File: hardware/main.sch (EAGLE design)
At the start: 79 parts, among them U1 TMS320F28069_PN_80, U10 TXB0101_DBV_6, U2 TXB0101_DBV_6, U3 SN74ABT541B_DW_20, U4 SN74LVC1G04_DBV_5, U5 SN74LVC4245A_DW_24, U7 Value, U8 Value, U9 SN74LVC4245A_DW_24

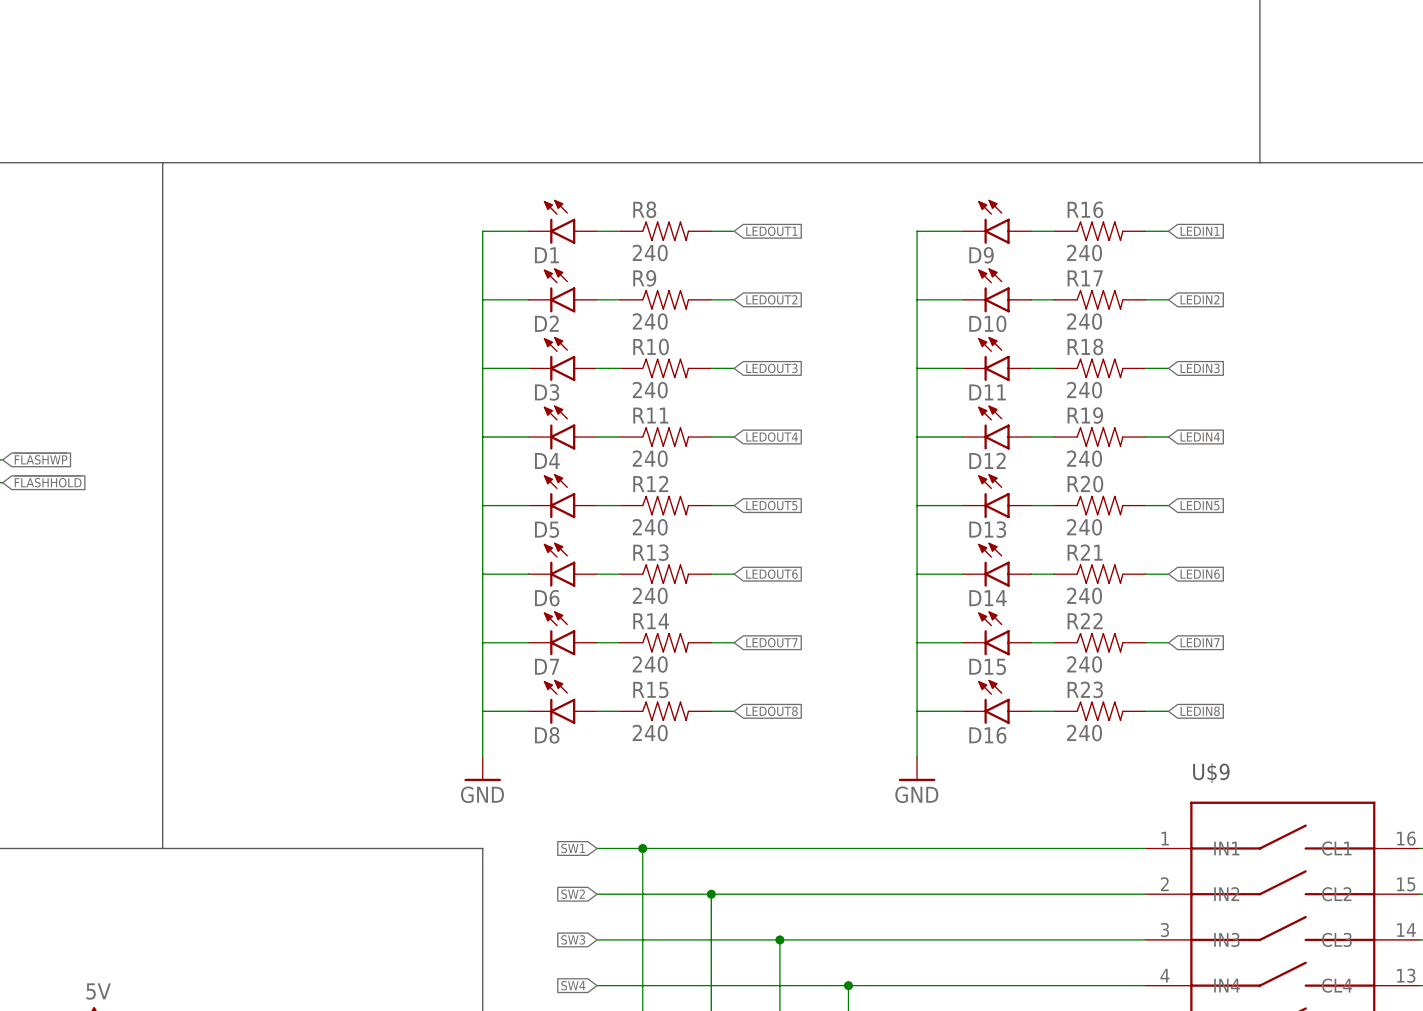
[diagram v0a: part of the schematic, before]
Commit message: Routed the output section. Ripped up SPI section. Finished routing input section.
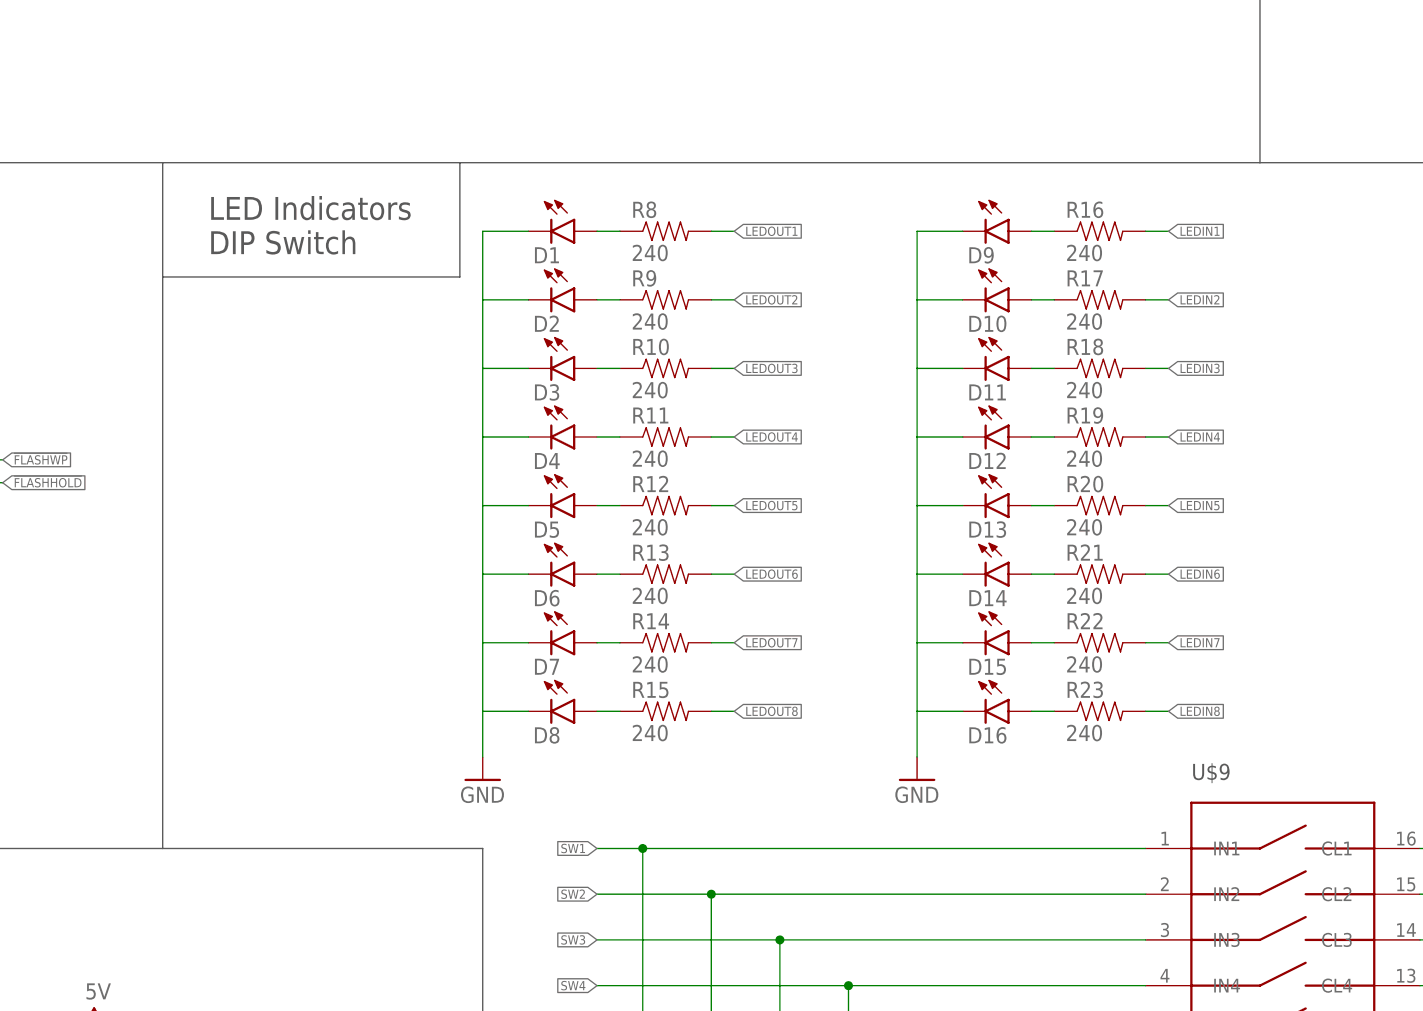
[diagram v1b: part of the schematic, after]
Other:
- note added: "LED Indicators DIP Switch"
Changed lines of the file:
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@@
 <setting verticaltext="up"/>
 </settings>
-<grid distance="0.1" unitdist="inch" unit="inch" style="lines" multiple="1" display="yes" altdistance="0.01" altunitdist="inch" altunit="inch"/>
+<grid distance="0.1" unitdist="inch" unit="inch" style="lines" multiple="1" display="no" altdistance="0.01" altunitdist="inch" altunit="inch"/>
 <layers>
 <layer number="1" name="Top" color="4" fill="1" visible="no" active="no"/>
@@
 <wire x1="363.22" y1="185.42" x2="398.78" y2="185.42" width="0.1524" layer="97"/>
 <wire x1="398.78" y1="185.42" x2="447.04" y2="185.42" width="0.1524" layer="97"/>
-<wire x1="447.04" y1="185.42" x2="447.04" y2="109.22" width="0.1524" layer="97"/>
+<wire x1="447.04" y1="185.42" x2="447.04" y2="172.72" width="0.1524" layer="97"/>
+<wire x1="447.04" y1="172.72" x2="447.04" y2="109.22" width="0.1524" layer="97"/>
 <wire x1="363.22" y1="172.72" x2="398.78" y2="172.72" width="0.1524" layer="97"/>
 <wire x1="398.78" y1="172.72" x2="398.78" y2="185.42" width="0.1524" layer="97"/>
@@
 <wire x1="320.04" y1="320.04" x2="568.96" y2="320.04" width="0.1524" layer="97"/>
 <wire x1="568.96" y1="320.04" x2="568.96" y2="185.42" width="0.1524" layer="97"/>
-<wire x1="568.96" y1="185.42" x2="447.04" y2="185.42" width="0.1524" layer="97"/>
+<wire x1="568.96" y1="185.42" x2="480.06" y2="185.42" width="0.1524" layer="97"/>
+<wire x1="480.06" y1="185.42" x2="447.04" y2="185.42" width="0.1524" layer="97"/>
 <wire x1="264.16" y1="297.18" x2="320.04" y2="297.18" width="0.1524" layer="97"/>
 <wire x1="320.04" y1="297.18" x2="320.04" y2="320.04" width="0.1524" layer="97"/>
@@
 <wire x1="599.44" y1="185.42" x2="599.44" y2="45.72" width="0.1524" layer="97"/>
 <wire x1="599.44" y1="45.72" x2="482.6" y2="45.72" width="0.1524" layer="97"/>
+<wire x1="447.04" y1="172.72" x2="480.06" y2="172.72" width="0.1524" layer="97"/>
+<wire x1="480.06" y1="172.72" x2="480.06" y2="185.42" width="0.1524" layer="97"/>
+<text x="452.12" y="175.26" size="2.54" layer="97">LED Indicators
+DIP Switch</text>
 </plain>
 <instances>

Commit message: Finished routing all signals traces. 3Vcc, 5Vcc, GND not yet routed. Signal traces need to be reviewed and cleaned up.
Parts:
- removed JP4: (no value), SparkFun-Connectors:M05PTH
- added R32, R33, R34, R35: 1K, SparkFun-Resistors:1KOHM-1/10W-1%(0603)
- added U$10, U$11: USER_SLIDE, ControllerCard:USER_SLIDE
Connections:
- new net N$29: R33.2, U$10.IN3
- new net N$38: R32.2, U$10.IN1
- new net N$39: R34.2, U$11.IN1
- new net N$40: R35.2, U$11.IN3
- net 3.3V: now also R34.1; no longer JP4.4
- net 5V: now also R32.1; no longer JP4.5
- net ENEXT: now also U1.GPIO20/EQEP1A/MDXA/COMP1OUT; no longer U1.GPIO4/EPWM3A
- net GND: now also R33.1, R35.1; no longer JP4.1
- net INSEL: now also U$10.OUT2; no longer JP4.3
- net RUNSEL: now also U$11.OUT2, U1.GPIO4/EPWM3A; no longer JP4.2, U1.GPIO20/EQEP1A/MDXA/COMP1OUT
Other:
- note added: "Slide Switches"
- note removed: "Slide Switch Connector"
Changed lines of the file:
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@@
 <part name="U3" library="ControllerCard" deviceset="SN74ABT541B_DW_20" device=""/>
 <part name="SUPPLY11" library="SparkFun-Aesthetics" deviceset="5V" device=""/>
-<part name="JP4" library="SparkFun-Connectors" deviceset="M05" device="PTH"/>
 <part name="SUPPLY13" library="SparkFun-Aesthetics" deviceset="5V" device=""/>
 <part name="U4" library="ControllerCard" deviceset="SN74LVC1G04_DBV_5" device=""/>
@@
 <part name="GND18" library="SparkFun-Aesthetics" deviceset="GND" device=""/>
 <part name="SUPPLY4" library="SparkFun-Aesthetics" deviceset="5V" device=""/>
+<part name="U$10" library="ControllerCard" deviceset="USER_SLIDE" device=""/>
+<part name="U$11" library="ControllerCard" deviceset="USER_SLIDE" device=""/>
+<part name="GND26" library="SparkFun-Aesthetics" deviceset="GND" device=""/>
+<part name="R32" library="SparkFun-Resistors" deviceset="1KOHM-1/10W-1%(0603)" device="" value="1K"/>
+<part name="R33" library="SparkFun-Resistors" deviceset="1KOHM-1/10W-1%(0603)" device="" value="1K"/>
+<part name="R34" library="SparkFun-Resistors" deviceset="1KOHM-1/10W-1%(0603)" device="" value="1K"/>
+<part name="R35" library="SparkFun-Resistors" deviceset="1KOHM-1/10W-1%(0603)" device="" value="1K"/>
 </parts>
 <sheets>
@@
 <wire x1="83.82" y1="276.86" x2="83.82" y2="294.64" width="0.1524" layer="97"/>
 <text x="53.34" y="284.48" size="2.54" layer="97">OUTPUT</text>
-<wire x1="449.58" y1="0" x2="482.6" y2="0" width="0.1524" layer="97"/>
-<wire x1="482.6" y1="0" x2="482.6" y2="45.72" width="0.1524" layer="97"/>
 <wire x1="449.58" y1="35.56" x2="477.52" y2="35.56" width="0.1524" layer="97"/>
 <wire x1="477.52" y1="35.56" x2="477.52" y2="45.72" width="0.1524" layer="97"/>
-<text x="454.66" y="38.1" size="2.54" layer="97">Slide Switch
-Connector</text>
 <text x="7.62" y="175.26" size="2.54" layer="97">Microcontroller</text>
 <wire x1="264.16" y1="294.64" x2="83.82" y2="294.64" width="0.1524" layer="97"/>
@@
 <wire x1="568.96" y1="185.42" x2="599.44" y2="185.42" width="0.1524" layer="97"/>
 <wire x1="599.44" y1="185.42" x2="599.44" y2="45.72" width="0.1524" layer="97"/>
-<wire x1="599.44" y1="45.72" x2="482.6" y2="45.72" width="0.1524" layer="97"/>
+<wire x1="599.44" y1="45.72" x2="558.8" y2="45.72" width="0.1524" layer="97"/>
+<wire x1="558.8" y1="45.72" x2="482.6" y2="45.72" width="0.1524" layer="97"/>
 <wire x1="447.04" y1="172.72" x2="480.06" y2="172.72" width="0.1524" layer="97"/>
 <wire x1="480.06" y1="172.72" x2="480.06" y2="185.42" width="0.1524" layer="97"/>
 <text x="452.12" y="175.26" size="2.54" layer="97">LED Indicators
 DIP Switch</text>
+<text x="452.12" y="38.1" size="2.54" layer="97">Slide Switches</text>
+<wire x1="449.58" y1="0" x2="558.8" y2="0" width="0.1524" layer="97"/>
+<wire x1="558.8" y1="0" x2="558.8" y2="45.72" width="0.1524" layer="97"/>
 </plain>
 <instances>
@@
 <instance part="R7" gate="G$1" x="248.92" y="264.16" rot="R90"/>
 <instance part="GND25" gate="1" x="248.92" y="254"/>
-<instance part="SUPPLY17" gate="G$1" x="472.44" y="25.4"/>
-<instance part="GND20" gate="1" x="469.9" y="10.16"/>
+<instance part="SUPPLY17" gate="G$1" x="508" y="25.4"/>
+<instance part="GND20" gate="1" x="508" y="7.62"/>
 <instance part="U$3" gate="G$1" x="292.1" y="78.74"/>
 <instance part="U$7" gate="G$1" x="335.28" y="71.12"/>
@@
 <instance part="U3" gate="A" x="373.38" y="236.22"/>
 <instance part="SUPPLY11" gate="G$1" x="434.34" y="238.76"/>
-<instance part="JP4" gate="G$1" x="457.2" y="20.32"/>
-<instance part="SUPPLY13" gate="G$1" x="467.36" y="27.94"/>
+<instance part="SUPPLY13" gate="G$1" x="457.2" y="25.4"/>
 <instance part="U4" gate="A" x="411.48" y="294.64"/>
 <instance part="SUPPLY23" gate="G$1" x="469.9" y="297.18"/>
@@
 <instance part="GND18" gate="1" x="563.88" y="53.34"/>
 <instance part="SUPPLY4" gate="G$1" x="589.28" y="111.76"/>
+<instance part="U$10" gate="G$1" x="482.6" y="17.78"/>
+<instance part="U$11" gate="G$1" x="533.4" y="17.78"/>
+<instance part="GND26" gate="1" x="457.2" y="7.62"/>
+<instance part="R32" gate="G$1" x="464.82" y="22.86"/>
+<instance part="R33" gate="G$1" x="464.82" y="12.7"/>
+<instance part="R34" gate="G$1" x="515.62" y="22.86"/>
+<instance part="R35" gate="G$1" x="515.62" y="12.7"/>
 </instances>
 <busses>
@@
 </segment>
 <segment>
-<pinref part="SUPPLY17" gate="G$1" pin="3.3V"/>
-<wire x1="464.82" y1="22.86" x2="472.44" y2="22.86" width="0.1524" layer="91"/>
-<wire x1="472.44" y1="22.86" x2="472.44" y2="25.4" width="0.1524" layer="91"/>
-<pinref part="JP4" gate="G$1" pin="4"/>
-</segment>
-<segment>
 <pinref part="SUPPLY12" gate="G$1" pin="3.3V"/>
 <pinref part="R6" gate="G$1" pin="2"/>
@@
 <pinref part="SUPPLY16" gate="G$1" pin="3.3V"/>
 <wire x1="462.28" y1="76.2" x2="462.28" y2="78.74" width="0.1524" layer="91"/>
+</segment>
+<segment>
+<pinref part="R34" gate="G$1" pin="1"/>
+<pinref part="SUPPLY17" gate="G$1" pin="3.3V"/>
+<wire x1="510.54" y1="22.86" x2="508" y2="22.86" width="0.1524" layer="91"/>
+<wire x1="508" y1="22.86" x2="508" y2="25.4" width="0.1524" layer="91"/>
 </segment>
 </net>
@@
 </segment>
 <segment>
-<pinref part="GND20" gate="1" pin="GND"/>
-<wire x1="464.82" y1="15.24" x2="469.9" y2="15.24" width="0.1524" layer="91"/>
-<wire x1="469.9" y1="15.24" x2="469.9" y2="12.7" width="0.1524" layer="91"/>
-<pinref part="JP4" gate="G$1" pin="1"/>
-</segment>
-<segment>
 <pinref part="GND14" gate="1" pin="GND"/>
 <pinref part="U$7" gate="G$1" pin="1"/>
@@
 <wire x1="553.72" y1="58.42" x2="553.72" y2="55.88" width="0.1524" layer="91"/>
 </segment>
+<segment>
+<pinref part="R33" gate="G$1" pin="1"/>
+<pinref part="GND26" gate="1" pin="GND"/>
+<wire x1="459.74" y1="12.7" x2="457.2" y2="12.7" width="0.1524" layer="91"/>
+<wire x1="457.2" y1="12.7" x2="457.2" y2="10.16" width="0.1524" layer="91"/>
+</segment>
+<segment>
+<pinref part="R35" gate="G$1" pin="1"/>
+<pinref part="GND20" gate="1" pin="GND"/>
+<wire x1="510.54" y1="12.7" x2="508" y2="12.7" width="0.1524" layer="91"/>
+<wire x1="508" y1="12.7" x2="508" y2="10.16" width="0.1524" layer="91"/>
+</segment>
 </net>
 <net name="TDI" class="0">
@@
 <pinref part="U3" gate="A" pin="VCC"/>
 <wire x1="434.34" y1="238.76" x2="434.34" y2="236.22" width="0.1524" layer="91"/>
-</segment>
-<segment>
-<pinref part="JP4" gate="G$1" pin="5"/>
-<pinref part="SUPPLY13" gate="G$1" pin="5V"/>
-<wire x1="464.82" y1="25.4" x2="467.36" y2="25.4" width="0.1524" layer="91"/>
-<wire x1="467.36" y1="25.4" x2="467.36" y2="27.94" width="0.1524" layer="91"/>
 </segment>
 <segment>
@@
 <wire x1="589.28" y1="73.66" x2="589.28" y2="78.74" width="0.1524" layer="91"/>
 </segment>
+<segment>
+<pinref part="R32" gate="G$1" pin="1"/>
+<pinref part="SUPPLY13" gate="G$1" pin="5V"/>
+<wire x1="459.74" y1="22.86" x2="457.2" y2="22.86" width="0.1524" layer="91"/>
+<wire x1="457.2" y1="22.86" x2="457.2" y2="25.4" width="0.1524" layer="91"/>
+</segment>
 </net>
 <net name="USBMON" class="0">
@@
 </segment>
 <segment>
-<pinref part="U1" gate="A" pin="GPIO4/EPWM3A"/>
-<wire x1="228.6" y1="35.56" x2="233.68" y2="35.56" width="0.1524" layer="91"/>
-<label x="233.68" y="35.56" size="1.016" layer="95" xref="yes"/>
+<pinref part="U1" gate="A" pin="GPIO20/EQEP1A/MDXA/COMP1OUT"/>
+<wire x1="45.72" y1="22.86" x2="40.64" y2="22.86" width="0.1524" layer="91"/>
+<label x="40.64" y="22.86" size="1.016" layer="95" rot="R180" xref="yes"/>
 </segment>
 </net>
@@
 <net name="INSEL" class="0">
 <segment>
-<wire x1="464.82" y1="20.32" x2="469.9" y2="20.32" width="0.1524" layer="91"/>
-<label x="469.9" y="20.32" size="1.016" layer="95" xref="yes"/>
-<pinref part="JP4" gate="G$1" pin="3"/>
+<wire x1="492.76" y1="17.78" x2="495.3" y2="17.78" width="0.1524" layer="91"/>
+<label x="495.3" y="17.78" size="1.016" layer="95" xref="yes"/>
+<pinref part="U$10" gate="G$1" pin="OUT2"/>
 </segment>
 <segment>
@@
 <net name="RUNSEL" class="0">
 <segment>
-<wire x1="464.82" y1="17.78" x2="469.9" y2="17.78" width="0.1524" layer="91"/>
-<label x="469.9" y="17.78" size="1.016" layer="95" xref="yes"/>
-<pinref part="JP4" gate="G$1" pin="2"/>
-</segment>
-<segment>
-<pinref part="U1" gate="A" pin="GPIO20/EQEP1A/MDXA/COMP1OUT"/>
-<wire x1="45.72" y1="22.86" x2="40.64" y2="22.86" width="0.1524" layer="91"/>
-<label x="40.64" y="22.86" size="1.016" layer="95" rot="R180" xref="yes"/>
+<wire x1="543.56" y1="17.78" x2="546.1" y2="17.78" width="0.1524" layer="91"/>
+<label x="546.1" y="17.78" size="1.016" layer="95" xref="yes"/>
+<pinref part="U$11" gate="G$1" pin="OUT2"/>
+</segment>
+<segment>
+<pinref part="U1" gate="A" pin="GPIO4/EPWM3A"/>
+<wire x1="228.6" y1="35.56" x2="233.68" y2="35.56" width="0.1524" layer="91"/>
+<label x="233.68" y="35.56" size="1.016" layer="95" xref="yes"/>
 </segment>
 </net>
@@
 </segment>
 </net>
+<net name="N$29" class="0">
+<segment>
+<pinref part="R33" gate="G$1" pin="2"/>
+<pinref part="U$10" gate="G$1" pin="IN3"/>
+<wire x1="469.9" y1="12.7" x2="472.44" y2="12.7" width="0.1524" layer="91"/>
+<wire x1="472.44" y1="12.7" x2="472.44" y2="15.24" width="0.1524" layer="91"/>
+</segment>
+</net>
+<net name="N$38" class="0">
+<segment>
+<pinref part="R32" gate="G$1" pin="2"/>
+<pinref part="U$10" gate="G$1" pin="IN1"/>
+<wire x1="469.9" y1="22.86" x2="472.44" y2="22.86" width="0.1524" layer="91"/>
+<wire x1="472.44" y1="22.86" x2="472.44" y2="20.32" width="0.1524" layer="91"/>
+</segment>
+</net>
+<net name="N$39" class="0">
+<segment>
+<pinref part="R34" gate="G$1" pin="2"/>
+<pinref part="U$11" gate="G$1" pin="IN1"/>
+<wire x1="520.7" y1="22.86" x2="523.24" y2="22.86" width="0.1524" layer="91"/>
+<wire x1="523.24" y1="22.86" x2="523.24" y2="20.32" width="0.1524" layer="91"/>
+</segment>
+</net>
+<net name="N$40" class="0">
+<segment>
+<pinref part="R35" gate="G$1" pin="2"/>
+<pinref part="U$11" gate="G$1" pin="IN3"/>
+<wire x1="520.7" y1="12.7" x2="523.24" y2="12.7" width="0.1524" layer="91"/>
+<wire x1="523.24" y1="12.7" x2="523.24" y2="15.24" width="0.1524" layer="91"/>
+</segment>
+</net>

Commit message: Finished cleaning up routing. Updated user connectors to have 10 pins.
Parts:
- added C3: 2.2UF, SparkFun-Capacitors:2.2UF50V10%(1206)
- C10, C11, C6, C7, C8, C9: value 2.2uF -> 2.2UF; device SparkFun-Capacitors:2.2UF-10V-20%(0603) -> SparkFun-Capacitors:2.2UF50V10%(1206)
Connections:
- net 3.3V: now also C10.1, C11.1, C3.1, C6.1, C7.1, C8.1, C9.1; no longer C10.2, C11.2, C6.2, C7.2, C8.2, C9.2
- net 5V: now also U$4.1, U$8.10
- net GND: now also C10.2, C11.2, C3.2, C6.2, C7.2, C8.2, C9.2, U$4.10, U$8.1; no longer C10.1, C11.1, C6.1, C7.1, C8.1, C9.1
- net N$13: now also U$4.2; no longer U$4.1
- net N$14: now also U$4.3; no longer U$4.2
- net N$15: now also U$4.4; no longer U$4.3
- net N$16: now also U$4.5; no longer U$4.4
- net N$17: now also U$4.9; no longer U$4.8
- net N$18: now also U$4.8; no longer U$4.7
- net N$19: now also U$4.7; no longer U$4.6
- net N$20: now also U$4.6; no longer U$4.5
- net N$21: now also U$8.9; no longer U$8.8
- net N$22: now also U$8.8; no longer U$8.7
- net N$23: now also U$8.7; no longer U$8.6
- net N$24: now also U$8.6; no longer U$8.5
- net N$25: now also U$8.2; no longer U$8.1
- net N$26: now also U$8.3; no longer U$8.2
- net N$27: now also U$8.4; no longer U$8.3
- net N$28: now also U$8.5; no longer U$8.4
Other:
- moved on the sheet: C10, C11, C6, C7, C8, C9, R32, R33, R34, R35

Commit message: Checked and edited component layouts. Updated and checked passive component values. Double checked chip peripherals.
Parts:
- added C13, C14, C15, C16: 0.1uF, SparkFun-Capacitors:1.0UF50V10%(1206)
- C4: value 0.22uF -> 0.47uF
- R5, R7: value 100/.25W -> 10K; device SparkFun-Resistors:100OHM-1/4W-5%(0603) -> SparkFun-Resistors:10KOHM-1/10W-1%(0603)0603
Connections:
- net 3.3V: now also C13.1, C15.1
- net 5V: now also C14.1, C16.1
- net GND: now also C13.2, C14.2, C15.2, C16.2; no longer U$2.IN
- net N$1: now also U$2.IN
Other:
- moved on the sheet: JP2, R1, R4, R5, U2
